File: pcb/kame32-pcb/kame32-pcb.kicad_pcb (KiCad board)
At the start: 2 copper layers, 62 x 29 mm, 15 parts, among them J2 Conn_02x04_Odd_Even, J3 Conn_01x04, J4 Conn_01x04, J5 Conn_01x02, J6 Conn_02x04_Odd_Even, SW1 SW_SPDT, U1 TEA1-0505

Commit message: PCB before DCDC change
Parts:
- removed ? (x2): , 
- removed the REF** at (151.1, 57.1)
- removed the REF** at (151.1, 34.3)
- added J1: Conn_01x06, Connector_PinHeader_2.54mm:PinHeader_1x06_P2.54mm_Vertical, F.Cu at (160.0, 35.6)
- added J7: Conn_01x05, Connector_PinHeader_2.54mm:PinHeader_1x05_P2.54mm_Vertical, F.Cu at (175.3, 55.9)
- added REF**: MountingHole_3mm, MountingHole:MountingHole_3mm, F.Cu at (214.8, 33.2)
- added REF**: MountingHole_3mm, MountingHole:MountingHole_3mm, F.Cu at (152.8, 58.2)
- added REF**: MountingHole_3mm, MountingHole:MountingHole_3mm, F.Cu at (152.8, 33.2)
- added REF**: MountingHole_3mm, MountingHole:MountingHole_3mm, F.Cu at (214.8, 58.2)
- moved J5 46.6 mm to (161.3, 55.9)
- moved R1 43.3 mm to (203.2, 33.0), turned to -90 degrees
- moved R2 33.4 mm to (200.7, 33.0), turned to -90 degrees
- moved U1 30.2 mm to (200.0, 43.7), turned to 0 degrees
- moved C1 20.7 mm to (209.5, 35.6), turned to 180 degrees
- moved SW1 12.3 mm to (214.6, 40.9), turned to -90 degrees
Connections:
- U2 pad 18: unconnected-(U2-D15-Pad18) -> Net-(J7-Pin_5)
- U2 pad 19: unconnected-(U2-D2-Pad19) -> Net-(J7-Pin_4)
- U2 pad 20: unconnected-(U2-D4-Pad20) -> Net-(J7-Pin_3)
- U2 pad 21: unconnected-(U2-RX2-Pad21) -> Net-(J7-Pin_2)
- U2 pad 22: unconnected-(U2-TX2-Pad22) -> Net-(J7-Pin_1)
- U2 pad 23: unconnected-(U2-D5-Pad23) -> Net-(J3-Pin_4)
- U2 pad 24: unconnected-(U2-D18-Pad24) -> Net-(J3-Pin_3)
- U2 pad 25: unconnected-(U2-D19-Pad25) -> Net-(J3-Pin_2)
- U2 pad 26: unconnected-(U2-D21-Pad26) -> Net-(J3-Pin_1)
- U2 pad 3: Net-(J3-Pin_1) -> Net-(J1-Pin_3)
- U2 pad 4: Net-(J3-Pin_2) -> Net-(J1-Pin_4)
- U2 pad 5: Net-(J3-Pin_3) -> Net-(J1-Pin_5)
- U2 pad 6: Net-(J3-Pin_4) -> Net-(J1-Pin_6)
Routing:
- net -BATT: track 103.6 -> 0.00 mm
- net +BATT: track 14.8 -> 57.5 mm
- net Net-(J3-Pin_1): track 36.6 -> 7.40 mm
- net Net-(J3-Pin_2): track 32.5 -> 11.0 mm
- net Net-(J3-Pin_3): track 29.0 -> 14.6 mm
- net +8V: track 71.3 -> 83.3 mm
- net Net-(J3-Pin_4): track 25.4 -> 18.2 mm
- net +6V: track 54.3 -> 48.7 mm
- net Net-(J7-Pin_5): track 0.00 -> 2.54 mm
- net Net-(J7-Pin_4): track 0.00 -> 2.54 mm
- net Net-(J7-Pin_3): track 0.00 -> 2.54 mm
- net Net-(J7-Pin_2): track 0.00 -> 2.54 mm
- net Net-(J7-Pin_1): track 0.00 -> 2.54 mm
- net Net-(J1-Pin_6): track 0.00 -> 2.54 mm
- net Net-(J1-Pin_5): track 0.00 -> 2.54 mm
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- added copper zone on B.Cu, net -BATT
- added copper zone on F.Cu, net -BATT
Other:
- board size 62 x 29 mm -> 67.6 x 30.6 mm
- board text added: "JavierIH.com CC BY-SA"
- board text added: "Kame32"
- board text added: "USB"
- board text added: "s"

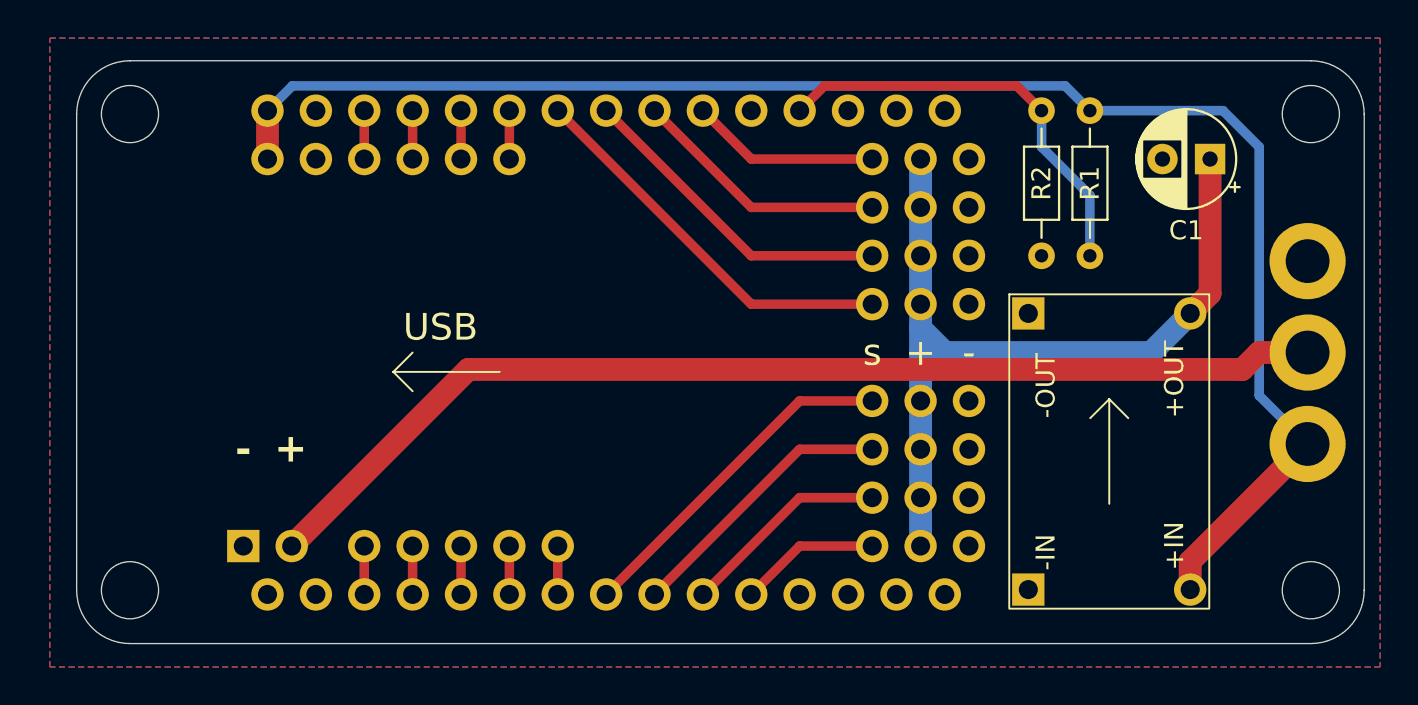
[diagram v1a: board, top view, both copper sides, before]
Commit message: esp32 pcb with servo headers
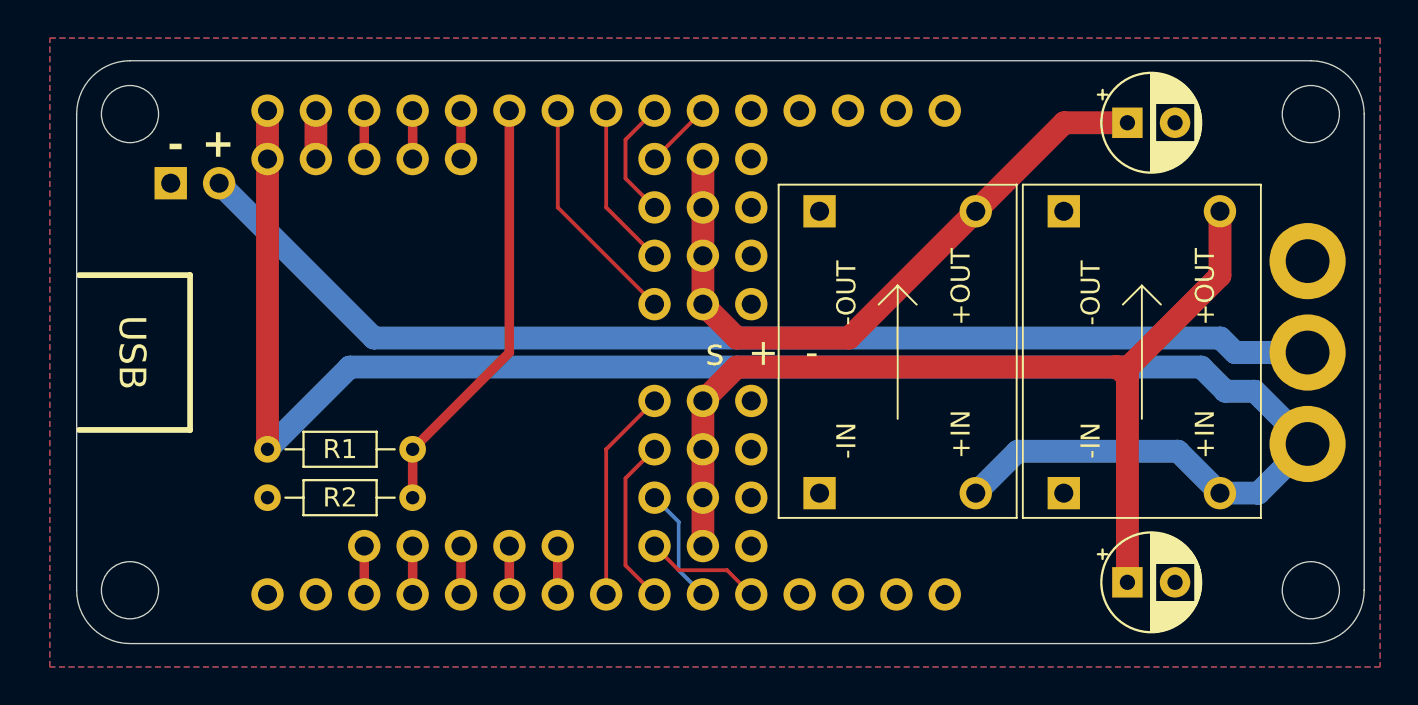
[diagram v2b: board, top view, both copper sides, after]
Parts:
- removed J1: Conn_01x06, Connector_PinHeader_2.54mm:PinHeader_1x06_P2.54mm_Vertical
- added C2: C, Capacitor_THT:CP_Radial_D5.0mm_P2.50mm, F.Cu at (205.2, 57.8)
- added G***: LOGO, LOGO, B.Cu at (165.0, 46.0)
- added J8: Conn_01x05, Connector_PinHeader_2.54mm:PinHeader_1x05_P2.54mm_Vertical, F.Cu at (160.0, 35.6)
- added U3: TEA1-0505, kame32:dcdc, F.Cu at (201.8, 38.3)
- U1: footprint Connector_PinHeader_2.54mm:PinHeader_2x02_P2.54mm_Vertical -> kame32:dcdc
- moved R1 46.7 mm to (160.0, 50.8), turned to 0 degrees
- moved R2 38.8 mm to (167.6, 53.3), turned to 180 degrees
- moved J5 19.4 mm to (157.5, 36.8)
- moved U1 12.2 mm to (189.0, 38.3)
- moved J2 11.4 mm to (182.9, 35.6)
- moved J3 11.4 mm to (180.3, 55.9)
- moved J4 11.4 mm to (180.3, 43.2)
- moved J6 11.4 mm to (182.9, 48.3)
- moved C1 4.74 mm to (205.2, 33.7), turned to 0 degrees
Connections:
- C1 pad 1: +6V -> /Vs1
- J2 pad 1: +6V -> /Vs1
- J2 pad 3: +6V -> /Vs1
- J2 pad 5: +6V -> /Vs1
- J2 pad 7: +6V -> /Vs1
- J6 pad 1: +6V -> /Vs2
- J6 pad 3: +6V -> /Vs2
- J6 pad 5: +6V -> /Vs2
- J6 pad 7: +6V -> /Vs2
- R1 pad 2: Net-(U2-D34) -> Net-(U2-D27)
- R2 pad 1: Net-(U2-D34) -> Net-(U2-D27)
- U1 pad 4: +6V -> /Vs1
- U2 pad 12: Net-(U2-D34) -> unconnected-(U2-D34-Pad12)
- U2 pad 6: Net-(J1-Pin_6) -> Net-(U2-D27)
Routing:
- net /Vs2: track 0.00 -> 53.1 mm
- net +6V: track 48.7 -> 0.00 mm
- net /Vs1: track 0.00 -> 35.3 mm
- net Net-(U2-D34): track 22.4 -> 0.00 mm
- net Net-(U2-D27): track 0.00 -> 22.4 mm
- net +8V: track 83.3 -> 97.1 mm
- net Net-(J4-Pin_2): track 17.1 -> 8.67 mm
- net Net-(J4-Pin_1): track 20.7 -> 12.3 mm
- net Net-(J4-Pin_3): track 13.5 -> 6.34 mm
- net Net-(J3-Pin_4): track 18.2 -> 11.2 mm
- net Net-(J4-Pin_4): track 9.94 -> 3.59 mm
- net Net-(J3-Pin_3): track 14.6 -> 8.88 mm
- net Net-(J3-Pin_2): track 11.0 -> 6.13 mm
- net +BATT: track 57.5 -> 60.8 mm
- net Net-(J1-Pin_6): track 2.54 -> 0.00 mm
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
